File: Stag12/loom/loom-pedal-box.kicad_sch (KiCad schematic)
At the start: 9 parts, among them J16 BPS SUPPLY, J17 Main I/O, J29 AT16-18PA-PM11

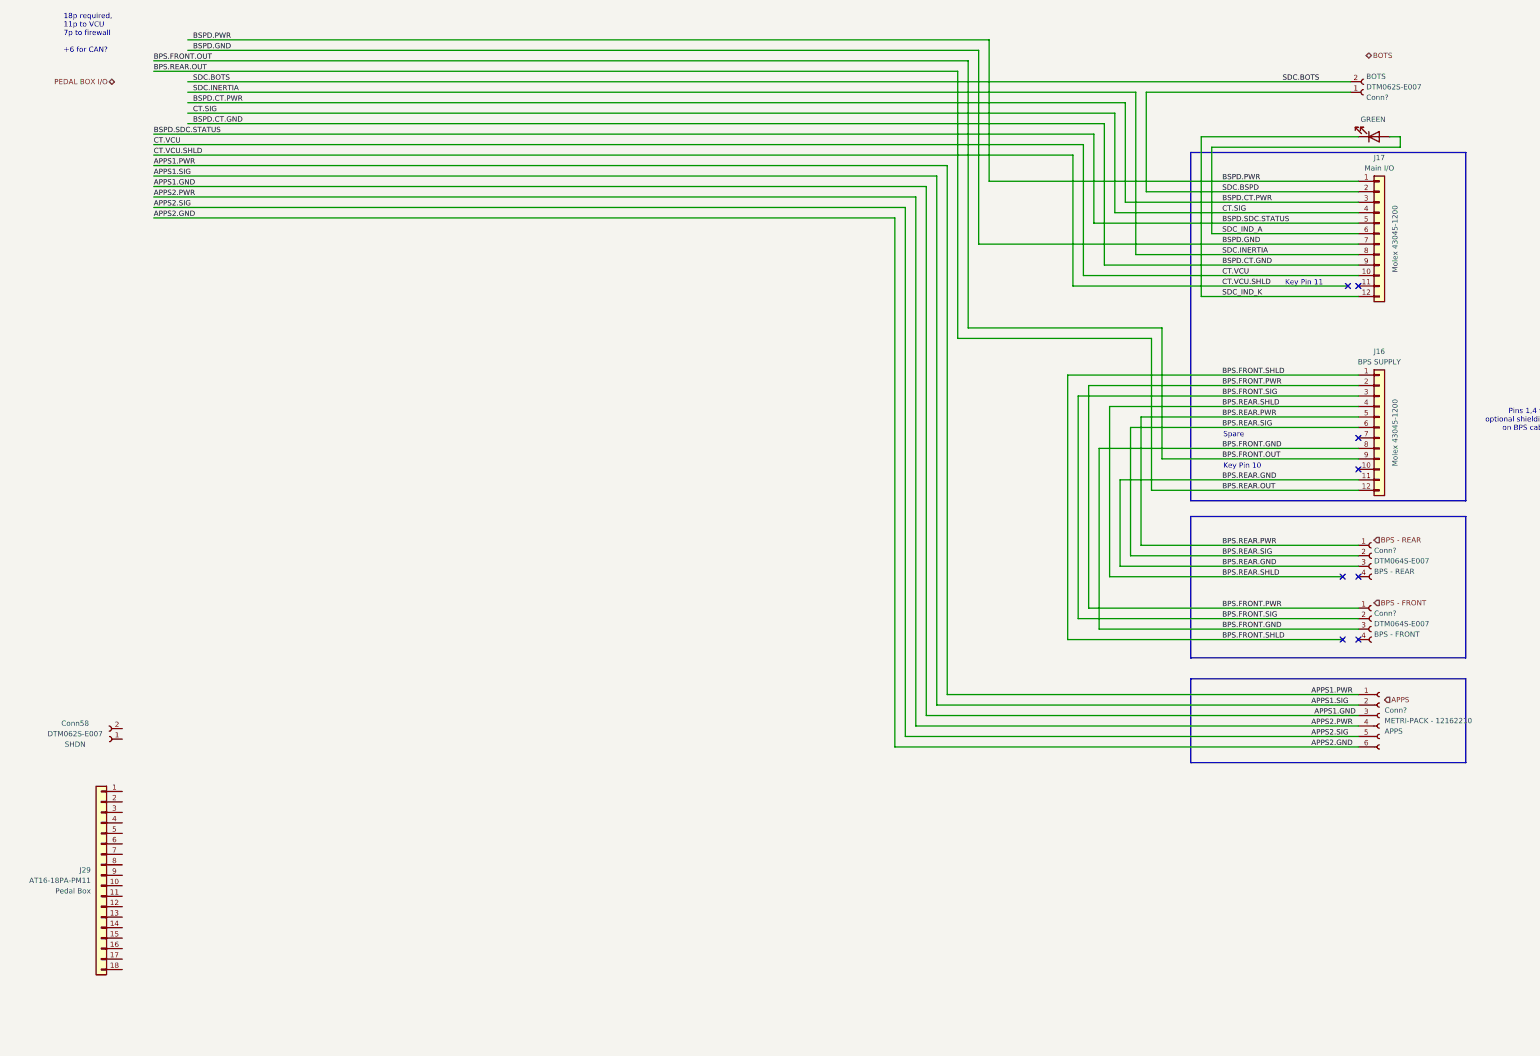
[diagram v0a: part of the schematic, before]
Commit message: Reserved Autosport for pedalbox
Pedal box loom near completion, pending connector spec

VCU is now connector hell
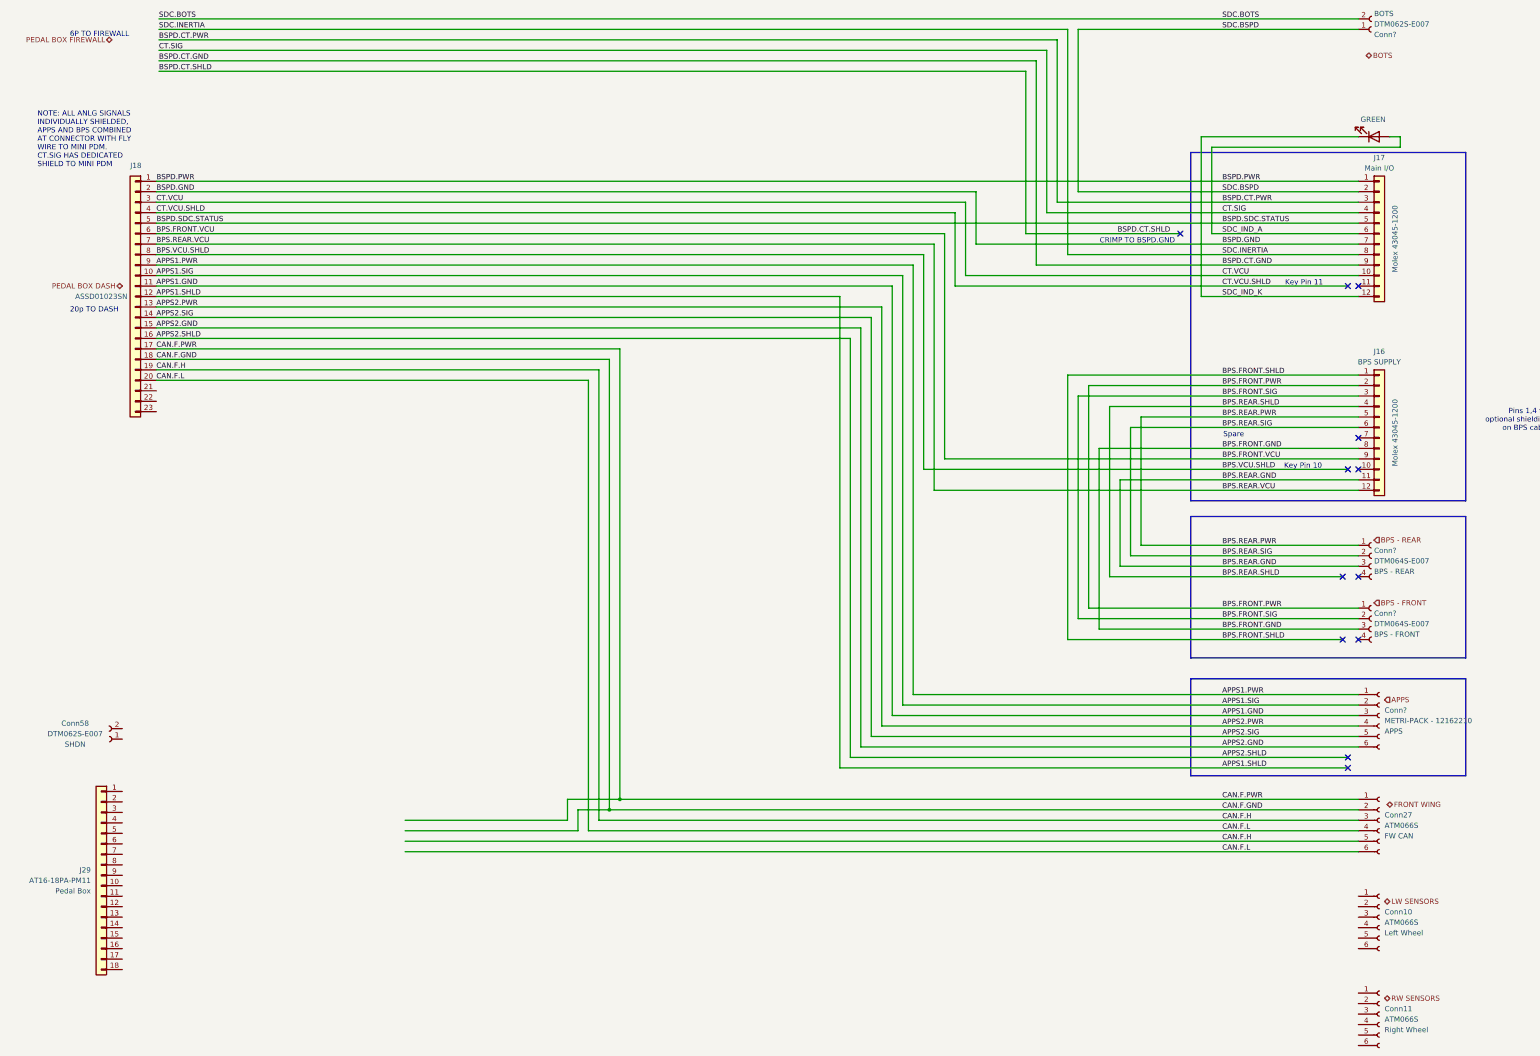
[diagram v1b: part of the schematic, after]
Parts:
- added Conn10, Conn11, Conn27: ATM066S, symbol Connector:Conn_01x06_Socket
- added J18: ASSD01023SN, symbol Connector_Generic:Conn_01x23
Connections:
- net APPS1.GND: now also J18.11 (Pin_11)
- net APPS1.PWR: now also J18.9 (Pin_9)
- net APPS1.SIG: now also J18.10 (Pin_10)
- net APPS2.GND: now also J18.15 (Pin_15)
- net APPS2.PWR: now also J18.13 (Pin_13)
- net APPS2.SIG: now also J18.14 (Pin_14)
- net BSPD.GND: now also J18.2 (Pin_2)
- net BSPD.PWR: now also J18.1 (Pin_1)
- net BSPD.SDC.STATUS: now also J18.5 (Pin_5)
- net CT.VCU: now also J18.3 (Pin_3)
- net CT.VCU.SHLD: now also J18.4 (Pin_4)
- net BPS.FRONT.OUT renamed BPS.FRONT.VCU
- net BPS.FRONT.VCU: now also J18.6 (Pin_6)
- net BPS.REAR.OUT renamed BPS.REAR.VCU
- net BPS.REAR.VCU: now also J18.7 (Pin_7)
- new net APPS1.SHLD: J18.12 (Pin_12)
- new net APPS2.SHLD: J18.16 (Pin_16)
- new net BPS.VCU.SHLD: J18.8 (Pin_8)
- new net CAN.F.GND: Conn27.2 (Pin_2), J18.18 (Pin_18)
- new net CAN.F.H: Conn27.3 (Pin_3), Conn27.5 (Pin_5), J18.19 (Pin_19)
- new net CAN.F.L: Conn27.4 (Pin_4), Conn27.6 (Pin_6), J18.20 (Pin_20)
- new net CAN.F.PWR: Conn27.1 (Pin_1), J18.17 (Pin_17)
- no-connect marks 8 -> 12
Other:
- note added: "20p TO DASH"
- note added: "6P TO FIREWALL"
- note added: "CRIMP TO BSPD.GND"
- note added: "NOTE: ALL ANLG SIGNALS INDIVIDUALLY SHIELDED, APPS AND BPS COMBINED AT CONNECTOR WITH FLY WIRE TO MINI PDM. CT.SIG HAS DEDICATED SHIELD TO MINI PDM"
- note removed: "18p required, 11p to VCU 7p to firewall +6 for CAN?"
- moved on the sheet: Conn?

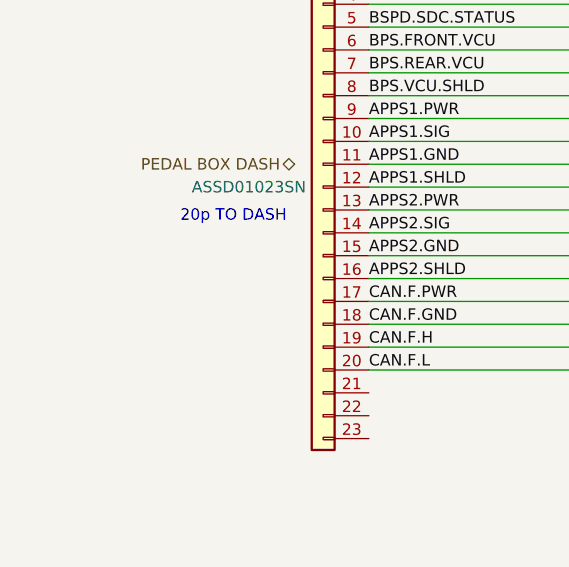
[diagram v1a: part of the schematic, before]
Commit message: Moved front loom connectors to correct locations
TODO: finish pinout, spec pedalbox connectors pending inventory
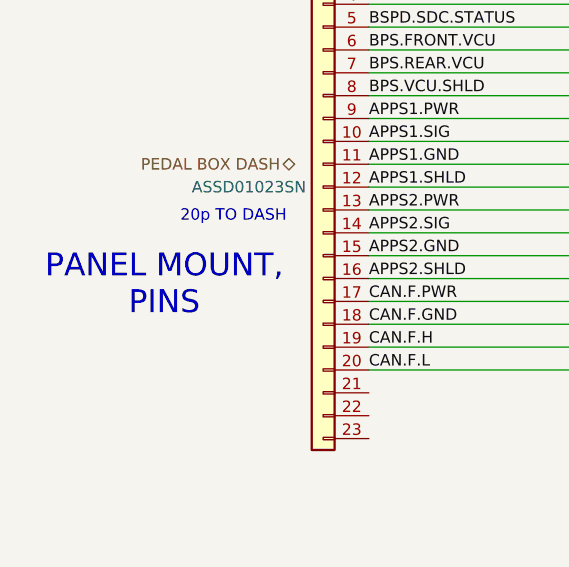
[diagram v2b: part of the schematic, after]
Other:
- note added: "PANEL MOUNT, PINS"
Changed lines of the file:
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@@
+		)
+	)
+	(text "PANEL MOUNT,\nPINS"
+		(exclude_from_sim no)
+		(at 27.432 98.552 0)
+		(effects
+			(font
+				(size 2.54 2.54)
+				(color 255 153 0 1)
+			)
 		)
 	)

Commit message: More progress on front loom
autosport my beloved
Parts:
- added Conn34: Deutsch_DTM_6P_Pin, symbol Connectors_SUFST:Deutsch_DTM_6P_Pin
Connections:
- net BSPD.CT.GND: now also Conn34.5
- net BSPD.CT.PWR: now also Conn34.3
- net BSPD.CT.SHLD: now also Conn34.6
- net CT.SIG: now also Conn34.4
- net SDC.INERTIA: now also Conn34.2
- net SDC.BOTS renamed SDC.FRONT
- net SDC.FRONT: now also Conn34.1
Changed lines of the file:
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@@
 		)
 	)
-	(label "SDC.BOTS"
+	(label "SDC.FRONT"
 		(at 50.8 20.32 0)
 		(effects
@@
 		)
 	)
-	(label "SDC.BOTS"
+	(label "SDC.FRONT"
 		(at 308.61 20.32 0)
 		(effects
@@
 	(hierarchical_label "PEDAL BOX FIREWALL"
 		(shape bidirectional)
-		(at 39.37 25.4 180)
+		(at 43.18 25.4 180)
 		(effects
 			(font
@@
 					(unit 1)
 				)
+			)
+		)
+	)
+	(symbol
+		(lib_id "Connectors_SUFST:Deutsch_DTM_6P_Pin")
+		(at 48.895 37.465 0)
+		(mirror x)
+		(unit 1)
+		(exclude_from_sim no)
+		(in_bom yes)
+		(on_board yes)
+		(dnp no)
+		(property "Reference" "Conn34"
+			(at 43.688 21.336 0)
+			(effects
+				(font
+					(size 1.27 1.27)
+				)
+				(justify right)
+			)
+		)
+		(property "Value" "Deutsch_DTM_6P_Pin"
+			(at 48.895 37.465 0)
+			(effects
+				(font
+					(size 1.27 1.27)
+				)
+				(hide yes)
+			)
+		)
+		(property "Footprint" ""
+			(at 48.895 37.465 0)
+			(effects
+				(font
+					(size 1.27 1.27)
+				)
+				(hide yes)
+			)
+		)
+		(property "Datasheet" ""
+			(at 48.895 37.465 0)
+			(effects
+				(font
+					(size 1.27 1.27)
+				)
+				(hide yes)
+			)
+		)
+		(property "Description" ""
+			(at 48.895 37.465 0)
+			(effects
+				(font
+					(size 1.27 1.27)
+				)
+				(hide yes)
+			)
+		)
+		(property "P/N" "DTM046P-E003"
+			(at 44.45 27.9399 0)
+			(effects
+				(font
+					(size 1.27 1.27)
+				)
+				(justify right)
+			)
+		)
+		(pin "1"
+		)
+		(pin "4"
+		)
+		(pin "2"
+		)
+		(pin "6"
+		)
+		(pin "5"
+		)
+		(pin "3"
+		)
+		(instances
+			(project ""
+				(path "/03011643-0690-4b85-ab78-d6a62dae52b1/f0d8d47c-6163-4e35-b09e-ddfb7232ae0a"
+					(reference "Conn34")
+					(unit 1)
+				)

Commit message: pedal box stuff and accu
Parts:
- removed Conn10, Conn11, Conn27: ATM066S, symbol Connector:Conn_01x06_Socket
- removed Conn58, Conn?: Deutsch_DTM_2S_Pin, symbol Connectors_SUFST:Deutsch_DTM_2S_Pin
- removed Conn?: METRI-PACK - 12162210, symbol Connector:Conn_01x06_Socket
- removed J29: AT16-18PA-PM11, symbol Connector_Generic:Conn_01x18
- added Conn112, Conn113: Deutsch_DTM_4S_Pin, symbol Connectors_SUFST:Deutsch_DTM_4S_Pin
- added Conn114: Deutsch_DTM_2S_Pin, symbol Connectors_SUFST:Deutsch_DTM_2S_Pin
- added Conn114: Conn_01x03_Socket, symbol Connector:Conn_01x03_Socket
- Conn? (x2): P/N DTM064S-E007 -> DTM04-4P
- J18: value ASSD01023SN -> 8STA01235PN; symbol Connector_Generic:Conn_01x23 -> Connector_Generic:Conn_01x22
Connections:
- net SDC.FRONT is gone; now on net SDC.BSPD: Conn34.1
- net APPS1.GND: now also Conn112.3
- net APPS1.PWR: now also Conn112.1
- net APPS1.SIG: now also Conn112.2
- net APPS2.GND: now also Conn113.3
- net APPS2.PWR: now also Conn113.1
- net APPS2.SIG: now also Conn113.2
- net CAN.F.GND renamed PEDALBOX.GND
- net CAN.F.PWR renamed PEDALBOX.PWR
- no-connect marks 12 -> 16
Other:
- note added: "APPS"
- note added: "BPS"
- note added: "BSPD"
- note added: "Damper Pots"
- note added: "Do not terminate shield here"
- note added: "Put BOTS before pedal box"
- note removed: "20p TO DASH"
- moved on the sheet: Conn34, Conn?, J16, J17

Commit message: Finish pedal box internal loom
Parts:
- added Conn10, Conn116: Conn_01x03_Socket, symbol Connector:Conn_01x05_Socket
- added Conn115: Conn_01x03_Socket, symbol Connector:Conn_01x03_Socket
- added J29, J61: Conn_01x12, symbol Connector_Generic:Conn_01x12
- added J62: Conn_01x12, symbol Connector_Generic:Conn_01x04
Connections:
- net CAN.F.H is gone; now on net APPS2.PWR: J18.19 (Pin_19)
- net CAN.F.L is gone; now on net APPS2.SIG: J18.20 (Pin_20)
- net PEDALBOX.GND is gone; now on net APPS1.SHLD: J18.18 (Pin_18)
- net PEDALBOX.PWR is gone; now on net APPS1.GND: J18.17 (Pin_17)
- net APPS1.GND: no longer J18.11 (Pin_11)
- net APPS1.PWR: now also J18.15 (Pin_15); no longer J18.9 (Pin_9)
- net APPS1.SHLD: no longer J18.12 (Pin_12)
- net APPS1.SIG: now also J18.16 (Pin_16); no longer J18.10 (Pin_10)
- net APPS2.GND: now also J18.21 (Pin_21); no longer J18.15 (Pin_15)
- net APPS2.PWR: no longer J18.13 (Pin_13)
- net APPS2.SHLD: now also J18.22 (Pin_22); no longer J18.16 (Pin_16)
- net APPS2.SIG: no longer J18.14 (Pin_14)
- net BSPD.SDC.STATUS: now also J61.1 (Pin_1); no longer J18.5 (Pin_5)
- net DAMPER.FL.SIG: now reaches Conn114.1 (Pin_1)
- net DAMPER.FL.SIG: now also J29.1 (Pin_1)
- net DAMPER.FL.PWR: now reaches Conn114.2 (Pin_2)
- net DAMPER.FL.PWR: now also J29.2 (Pin_2)
- net DAMPER.FL.GND: now reaches Conn114.3 (Pin_3)
- net DAMPER.FL.GND: now also J29.3 (Pin_3)
- new net BOTS.SDC.STATUS: J18.5 (Pin_5), J61.4 (Pin_4)
- new net CAN.S.H: J18.11 (Pin_11), J18.13 (Pin_13), J62.3 (Pin_3)
- new net CAN.S.L: J18.12 (Pin_12), J18.14 (Pin_14), J62.4 (Pin_4)
- new net DAMPER.FR.GND: Conn115.3 (Pin_3), J29.6 (Pin_6)
- new net DAMPER.FR.PWR: Conn115.2 (Pin_2), J29.5 (Pin_5)
- new net DAMPER.FR.SIG: Conn115.1 (Pin_1), J29.4 (Pin_4)
- new net FRONTSENSORS.GND: J18.10 (Pin_10), J62.1 (Pin_1)
- new net FRONTSENSORS.PWR: J18.9 (Pin_9), J62.2 (Pin_2)
- no-connect marks 16 -> 14
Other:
- note added: "8Ch Sensor Hub"
- note added: "ADC GND 3V3"
- note added: "Accelerator Pedal Position Sensor"
- note added: "BSPD PCB"
- note added: "Brake Pressure Sensor"
- note added: "Do not terminate shield here!"
- note added: "GND +GLV CANH CANL"
- note added: "Molex 43045-1200"
- note added: "NOTE: ALL ANLG SIGNALS INDIVIDUALLY SHIELDED, APPS AND BPS COMBINED AT CONNECTOR WITH FLY WIRE TO SENSOR PDM. CT.SIG HAS DEDICATED SHIELD TO SENSOR PDM"
- note added: "Splice in connector"
- note added: "Vehicle Performance Sensors"
- note removed: "APPS"
- note removed: "BPS"
- note removed: "BSPD"
- note removed: "Damper Pots"
- note removed: "Do not terminate shield here"
- note removed: "NOTE: ALL ANLG SIGNALS INDIVIDUALLY SHIELDED, APPS AND BPS COMBINED AT CONNECTOR WITH FLY WIRE TO MINI PDM. CT.SIG HAS DEDICATED SHIELD TO MINI PDM"
- note removed: "PANEL MOUNT, PINS"
- company: (none) -> SUFST
- moved on the sheet: Conn112, Conn113, Conn114, Conn?, J18

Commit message: Dash box pinout
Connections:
- net APPS1.SHLD: now also Conn112.4
- net APPS2.SHLD: now also Conn113.4
- net BPS.FRONT.SHLD: now also Conn?.4
- net BPS.REAR.SHLD: now also Conn?.4
- net BOTS.SDC.STATUS renamed GPS.PPS2
- no-connect marks 14 -> 6
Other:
- note added: "Do not terminate shield at sensor!"
- note removed: "Do not terminate shield here!"
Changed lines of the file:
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@@
 		)
 	)
-	(text "Do not terminate shield here!"
+	(text "Do not terminate shield at sensor!"
 		(exclude_from_sim no)
 		(at 401.32 247.65 0)
@@
 		)
 	)
-	(text "Do not terminate shield here!"
+	(text "Do not terminate shield at sensor!"
 		(exclude_from_sim no)
 		(at 401.32 203.2 0)
@@
 	)
 	(no_connect
-		(at 408.94 184.15)
-	)
-	(no_connect
-		(at 408.94 199.39)
-	)
-	(no_connect
 		(at 412.75 101.6)
-	)
-	(no_connect
-		(at 414.02 243.84)
-	)
-	(no_connect
-		(at 414.02 227.33)
 	)
 	(no_connect
@@
 	)
 	(no_connect
-		(at 412.75 199.39)
-	)
-	(no_connect
-		(at 408.94 243.84)
-	)
-	(no_connect
-		(at 412.75 184.15)
-	)
-	(no_connect
 		(at 410.21 101.6)
 	)
-	(no_connect
-		(at 408.94 227.33)
-	)
 	(wire
 		(pts
@@
 	(wire
 		(pts
-			(xy 297.18 227.33) (xy 408.94 227.33)
+			(xy 297.18 227.33) (xy 414.02 227.33)
 		)
 		(stroke
@@
 	(wire
 		(pts
-			(xy 287.02 243.84) (xy 408.94 243.84)
+			(xy 287.02 243.84) (xy 414.02 243.84)
 		)
 		(stroke
@@
 	(wire
 		(pts
-			(xy 353.06 184.15) (xy 408.94 184.15)
+			(xy 353.06 184.15) (xy 412.75 184.15)
 		)
 		(stroke
@@
 	(wire
 		(pts
-			(xy 342.9 199.39) (xy 408.94 199.39)
+			(xy 342.9 199.39) (xy 412.75 199.39)
 		)
 		(stroke
@@
 	(wire
 		(pts
+			(xy 134.62 320.04) (xy 195.58 320.04)
+		)
+		(stroke
+			(width 0)
+			(type default)
+		)
+	)
+	(wire
+		(pts
 			(xy 345.44 194.31) (xy 412.75 194.31)
-		)
-		(stroke
-			(width 0)
-			(type default)
-		)
-	)
-	(wire
-		(pts
-			(xy 195.58 320.04) (xy 134.62 320.04)
 		)
 		(stroke
@@
 	)
 	(label "DAMPER.FL.SIG"
-		(at 161.29 270.51 180)
-		(effects
-			(font
-				(size 1.27 1.27)
-			)
-			(justify right bottom)
+		(at 145.415 270.51 0)
+		(effects
+			(font
+				(size 1.27 1.27)
+			)
+			(justify left bottom)
 		)
 	)
@@
 	)
 	(label "DAMPER.FL.PWR"
-		(at 161.29 273.05 180)
-		(effects
-			(font
-				(size 1.27 1.27)
-			)
-			(justify right bottom)
+		(at 145.415 273.05 0)
+		(effects
+			(font
+				(size 1.27 1.27)
+			)
+			(justify left bottom)
 		)
 	)
@@
 	)
 	(label "BSPD.SDC.STATUS"
-		(at 161.29 312.42 180)
-		(effects
-			(font
-				(size 1.27 1.27)
-			)
-			(justify right bottom)
+		(at 145.415 312.42 0)
+		(effects
+			(font
+				(size 1.27 1.27)
+			)
+			(justify left bottom)
 		)
 	)
@@
 	)
 	(label "DAMPER.FR.GND"
-		(at 161.29 283.21 180)
-		(effects
-			(font
-				(size 1.27 1.27)
-			)
-			(justify right bottom)
+		(at 145.415 283.21 0)
+		(effects
+			(font
+				(size 1.27 1.27)
+			)
+			(justify left bottom)
 		)
 	)
@@
 	)
 	(label "DAMPER.FL.GND"
-		(at 161.29 275.59 180)
-		(effects
-			(font
-				(size 1.27 1.27)
-			)
-			(justify right bottom)
+		(at 145.415 275.59 0)
+		(effects
+			(font
+				(size 1.27 1.27)
+			)
+			(justify left bottom)
 		)
 	)
@@
 		)
 	)
-	(label "BOTS.SDC.STATUS"
-		(at 161.29 320.04 180)
-		(effects
-			(font
-				(size 1.27 1.27)
-			)
-			(justify right bottom)
+	(label "GPS.PPS2"
+		(at 145.415 320.04 0)
+		(effects
+			(font
+				(size 1.27 1.27)
+			)
+			(justify left bottom)
 		)
 	)
@@
 	)
 	(label "DAMPER.FR.SIG"
-		(at 161.29 278.13 180)
-		(effects
-			(font
-				(size 1.27 1.27)
-			)
-			(justify right bottom)
+		(at 145.415 278.13 0)
+		(effects
+			(font
+				(size 1.27 1.27)
+			)
+			(justify left bottom)
 		)
 	)
 	(label "DAMPER.FR.PWR"
-		(at 161.29 280.67 180)
-		(effects
-			(font
-				(size 1.27 1.27)
-			)
-			(justify right bottom)
+		(at 145.415 280.67 0)
+		(effects
+			(font
+				(size 1.27 1.27)
+			)
+			(justify left bottom)
 		)
 	)
@@
 		)
 	)
-	(label "BOTS.SDC.STATUS"
+	(label "GPS.PPS2"
 		(at 121.92 86.36 0)
 		(effects

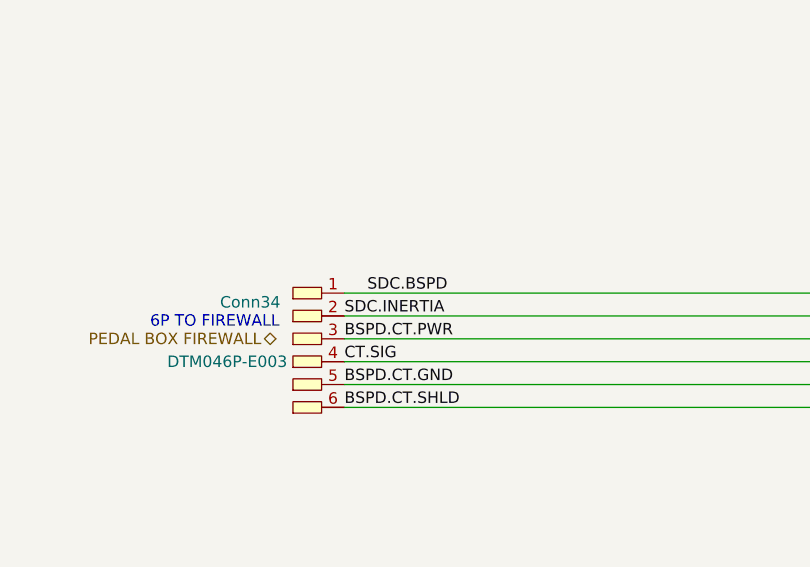
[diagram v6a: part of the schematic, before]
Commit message: Just one more Front Loom
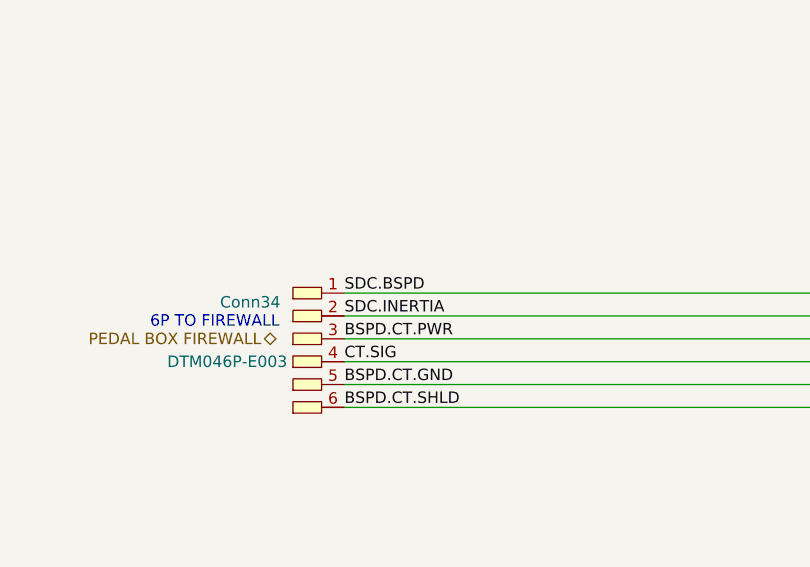
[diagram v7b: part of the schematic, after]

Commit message: extra power on accu + front loom redraw
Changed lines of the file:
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@@
 	(text "NOTE: ALL ANLG SIGNALS\nINDIVIDUALLY SHIELDED,\nAPPS AND BPS COMBINED\nAT CONNECTOR WITH FLY\nWIRE TO SENSOR PDM.\nCT.SIG HAS DEDICATED\nSHIELD TO SENSOR PDM"
 		(exclude_from_sim no)
-		(at 83.82 73.66 0)
+		(at 66.04 76.962 0)
 		(effects
 			(font
